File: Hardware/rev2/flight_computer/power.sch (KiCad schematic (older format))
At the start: 48 parts, among them U6 Buck_Converter_2, U7 LDO_600MA, U8 LP5907QMFX-3.3, U9 LP5907QMFX-3.3

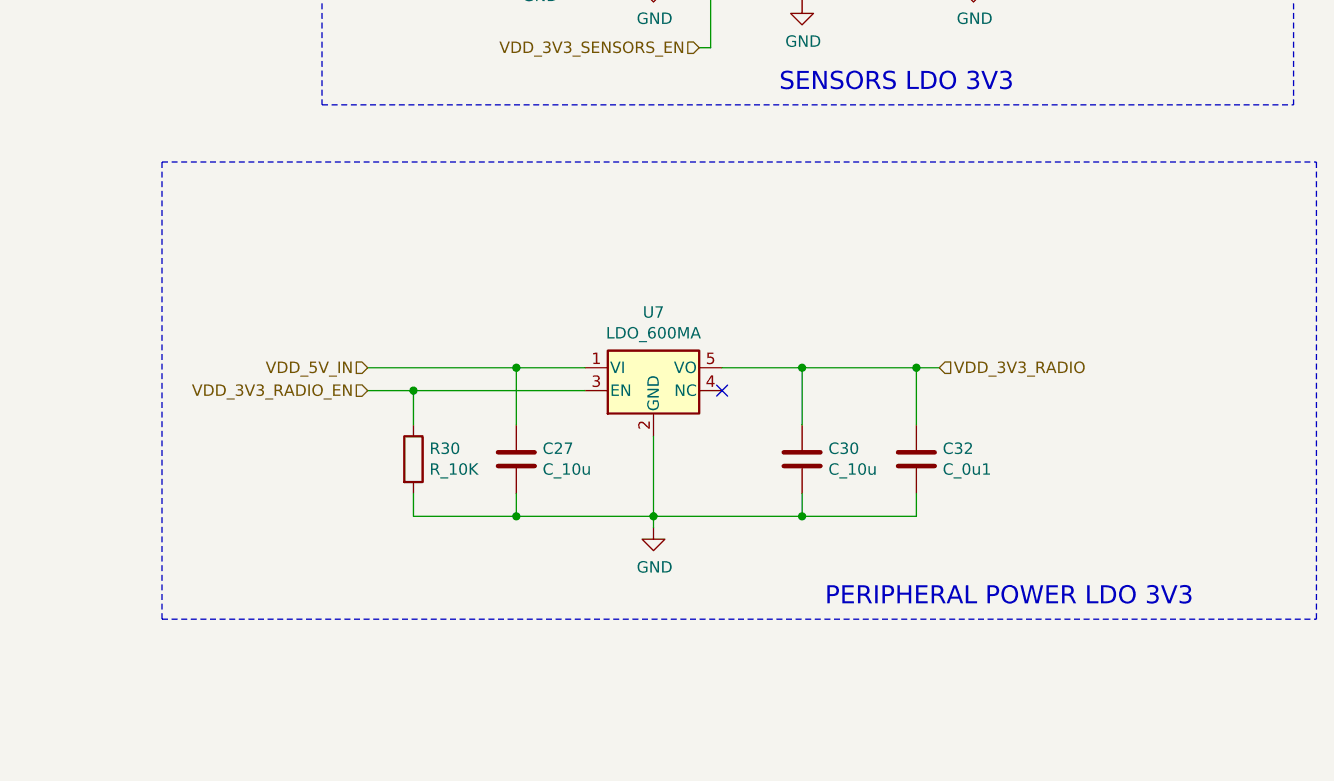
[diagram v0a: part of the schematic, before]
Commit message: Removes frysky + spektrum connectors
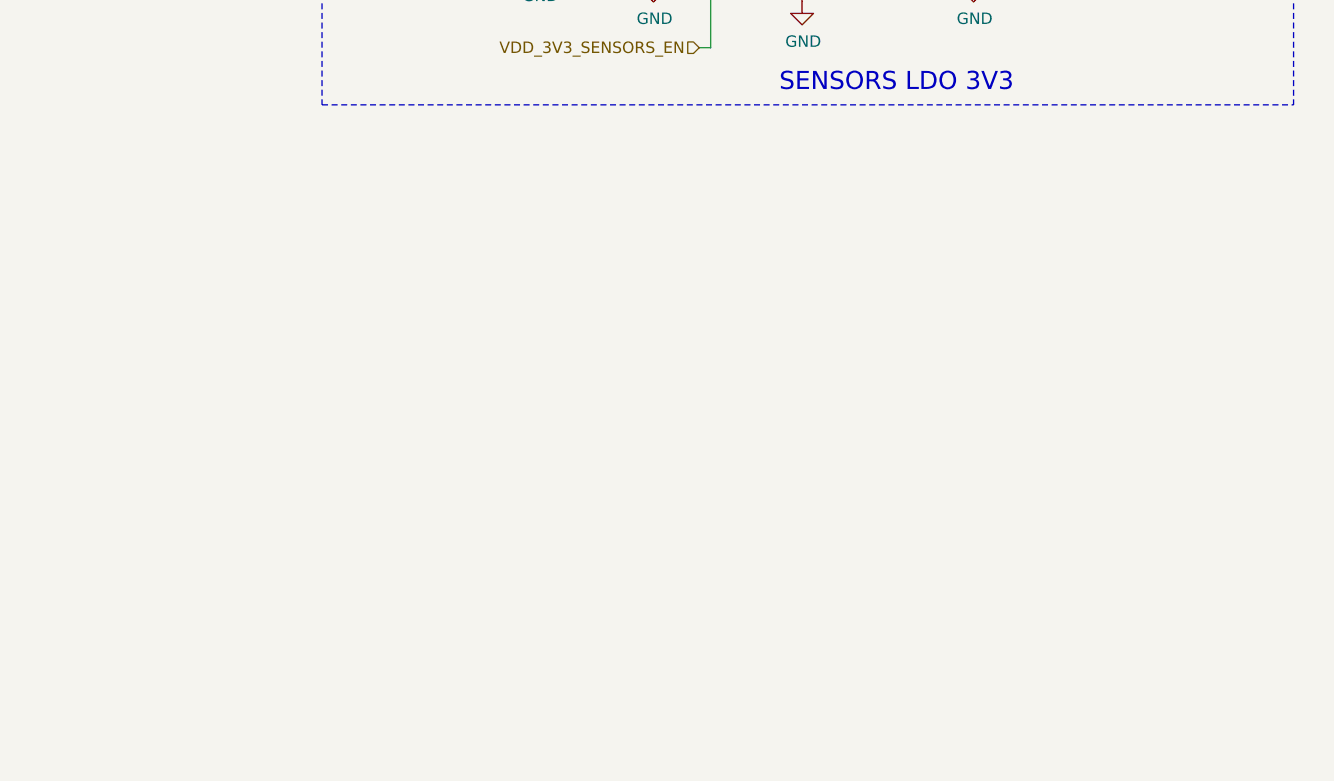
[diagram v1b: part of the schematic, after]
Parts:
- removed C27, C30: C_10u, Capacitors_SMD:C_0805, symbol openDrone_parts:C_10u
- removed C32: C_0u1, Capacitors_SMD:C_0805, symbol openDrone_parts:C_0u1
- removed R30: R_10K, Resistors_SMD:R_0805, symbol openDrone_parts:R_10K
- removed U7: LDO_600MA, drone_footprints:SOT-25_DIO, symbol openDrone_parts:LDO_600MA
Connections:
- no-connect marks 1 -> 0
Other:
- note removed: "PERIPHERAL POWER LDO 3V3"
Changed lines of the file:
@@
 	1    0    0    -1
 $EndComp
-$Comp
-L openDrone_parts:LDO_600MA U?
-U 1 1 5F8D4287
-P 12900 5300
-AR Path="/5F615F42/5F8D4287" Ref="U?"  Part="1"
-AR Path="/5F84A65B/5F8D4287" Ref="U7"  Part="1"
-F 0 "U7" H 12900 5542 50  0000 C CNN
-F 1 "LDO_600MA" H 12900 5451 50  0000 C CNN
-F 2 "drone_footprints:SOT-25_DIO" H 13400 5850 50  0001 C CIN
-F 3 "" H 12900 5250 50  0001 C CNN
-F 4 "AP7365-33WG-7DICT-ND" H 13300 5750 50  0001 C CNN "DPN"
-F 5 "AP7365-33WG-7" H 13300 5700 50  0001 C CNN "MPN"
-	1    12900 5300
-	1    0    0    -1
-$EndComp
-Text HLabel 11650 5300 0    50   Input ~ 0
-VDD_5V_IN
-$Comp
-L openDrone_parts:C_10u C?
-U 1 1 5F8D428F
-P 12300 5700
-AR Path="/5F615F42/5F8D428F" Ref="C?"  Part="1"
-AR Path="/5F84A65B/5F8D428F" Ref="C27"  Part="1"
-F 0 "C27" H 12415 5746 50  0000 L CNN
-F 1 "C_10u" H 12415 5655 50  0000 L CNN
-F 2 "Capacitors_SMD:C_0805" H 12338 5550 50  0001 C CNN
-F 3 "" H 12325 5800 50  0001 C CNN
-F 4 "490-16824-1-ND" H 12300 5700 60  0001 C CNN "DPN"
-	1    12300 5700
-	1    0    0    -1
-$EndComp
-$Comp
-L openDrone_parts:R_10K R?
-U 1 1 5F8D4296
-P 11850 5700
-AR Path="/5F615F42/5F8D4296" Ref="R?"  Part="1"
-AR Path="/5F84A65B/5F8D4296" Ref="R30"  Part="1"
-F 0 "R30" V 11804 5770 50  0000 L CNN
-F 1 "R_10K" V 11895 5770 50  0000 L CNN
-F 2 "Resistors_SMD:R_0805" H 11050 5850 50  0001 C CNN
-F 3 "" H 11550 6200 50  0001 C CNN
-F 4 "311-10.0KCRCT-ND" H 11200 5950 60  0001 C CNN "DPN"
-	1    11850 5700
-	0    1    1    0
-$EndComp
-$Comp
-L power:GND #PWR?
-U 1 1 5F8D429C
-P 12900 6000
-AR Path="/5F615F42/5F8D429C" Ref="#PWR?"  Part="1"
-AR Path="/5F84A65B/5F8D429C" Ref="#PWR043"  Part="1"
-F 0 "#PWR043" H 12900 5750 50  0001 C CNN
-F 1 "GND" H 12905 5827 50  0000 C CNN
-F 2 "" H 12900 6000 50  0001 C CNN
-F 3 "" H 12900 6000 50  0001 C CNN
-	1    12900 6000
-	1    0    0    -1
-$EndComp
-Wire Wire Line
-	12900 6000 12900 5950
-Wire Wire Line
-	12300 5850 12300 5950
-Wire Wire Line
-	12300 5950 12900 5950
-Connection ~ 12900 5950
-Wire Wire Line
-	12900 5950 12900 5600
-Wire Wire Line
-	11850 5850 11850 5950
-Wire Wire Line
-	11850 5950 12300 5950
-Connection ~ 12300 5950
-Wire Wire Line
-	11650 5300 12300 5300
-Wire Wire Line
-	12300 5550 12300 5300
-Connection ~ 12300 5300
-Wire Wire Line
-	12300 5300 12600 5300
-Wire Wire Line
-	11650 5400 11850 5400
-Wire Wire Line
-	11850 5550 11850 5400
-Connection ~ 11850 5400
-Wire Wire Line
-	11850 5400 12600 5400
-$Comp
-L openDrone_parts:C_10u C?
-U 1 1 5F8D42B4
-P 13550 5700
-AR Path="/5F615F42/5F8D42B4" Ref="C?"  Part="1"
-AR Path="/5F84A65B/5F8D42B4" Ref="C30"  Part="1"
-F 0 "C30" H 13665 5746 50  0000 L CNN
-F 1 "C_10u" H 13665 5655 50  0000 L CNN
-F 2 "Capacitors_SMD:C_0805" H 13588 5550 50  0001 C CNN
-F 3 "" H 13575 5800 50  0001 C CNN
-F 4 "490-16824-1-ND" H 13550 5700 60  0001 C CNN "DPN"
-	1    13550 5700
-	1    0    0    -1
-$EndComp
-$Comp
-L openDrone_parts:C_0u1 C?
-U 1 1 5F8D42BB
-P 14050 5700
-AR Path="/5F615F42/5F8D42BB" Ref="C?"  Part="1"
-AR Path="/5F84A65B/5F8D42BB" Ref="C32"  Part="1"
-F 0 "C32" H 14165 5746 50  0000 L CNN
-F 1 "C_0u1" H 14165 5655 50  0000 L CNN
-F 2 "Capacitors_SMD:C_0805" H 14088 5550 50  0001 C CNN
-F 3 "https://www.digikey.com/product-detail/en/kemet/C0805C104Z4VACTU/399-9159-1-ND/3522677" H 14075 5800 50  0001 C CNN
-F 4 "478-3352-1-ND" H 14050 5700 60  0001 C CNN "DPN"
-	1    14050 5700
-	1    0    0    -1
-$EndComp
-Wire Wire Line
-	13550 5850 13550 5950
-Wire Wire Line
-	13550 5950 12900 5950
-Wire Wire Line
-	14050 5850 14050 5950
-Wire Wire Line
-	14050 5950 13550 5950
-Connection ~ 13550 5950
-Wire Wire Line
-	13200 5300 13550 5300
-Wire Wire Line
-	14050 5300 14050 5550
-Wire Wire Line
-	13550 5550 13550 5300
-Connection ~ 13550 5300
-Wire Wire Line
-	13550 5300 14050 5300
-Text HLabel 14150 5300 2    50   Input ~ 0
-VDD_3V3_RADIO
 Text Notes 14850 2650 0    79   ~ 0
 STM LDO 3V3
@@
 Text HLabel 1350 3300 0    50   Input ~ 0
 VDD_5V_USB
-Text Notes 13650 6350 0    79   ~ 0
-PERIPHERAL POWER LDO 3V3
-Wire Notes Line
-	10750 4400 10750 6400
 Wire Notes Line
 	6350 750  6350 2550
@@
 Text Label 1350 4100 2    50   ~ 0
 VDD_5V_BUCK
-Wire Notes Line
-	10750 4400 15800 4400
-Wire Notes Line
-	10750 6400 15800 6400
-Wire Notes Line
-	15800 4400 15800 6400
-Text HLabel 11650 5400 0    50   Input ~ 0
-VDD_3V3_RADIO_EN
 Wire Wire Line
 	3850 1150 4000 1150
@@
 	4300 1250 4300 1150
 Connection ~ 4300 1150
-Connection ~ 14050 5300
-Wire Wire Line
-	14050 5300 14150 5300
 $Comp
 L openDrone_parts:LED_0805_Green D5
@@
 	0    1    1    0
 $EndComp
-NoConn ~ 13200 5400
 $EndSCHEMATC

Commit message: added new buck converter schematic
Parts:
- added C?: C_22u, drone_footprints:C_0805, symbol personal:C_22u
- added R?: R_2K18, personal:R_0805, symbol personal:R_2K18
- added U?: OKL-T_1-W12P-C, personal:OKL-T1-W12P-C, symbol personal:OKL-T_1-W12P-C
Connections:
- net GND: now also C?.2, R?.2, U?.11 (GND), U?.3 (GND), U?.7 (GND)
- net VBAT: now also C?.1, U?.2 (VIN)
- net VDD_5V_BUCK: now also U?.4 (VOUT)
- new net: R?.1, U?.6 (TRIM)
- no-connect marks 0 -> 1
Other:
- note added: "BUCK CONVERTER 5-14V, 2A"
- note added: "OLD BUCK CONVERTER 8-25V, 3A"
- note removed: "BUCK CONVERTER 8-25V, 3A"
- moved on the sheet: C18, C20, C21, C22, C23, C24, C25, L2, R15, R16, R23, R26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

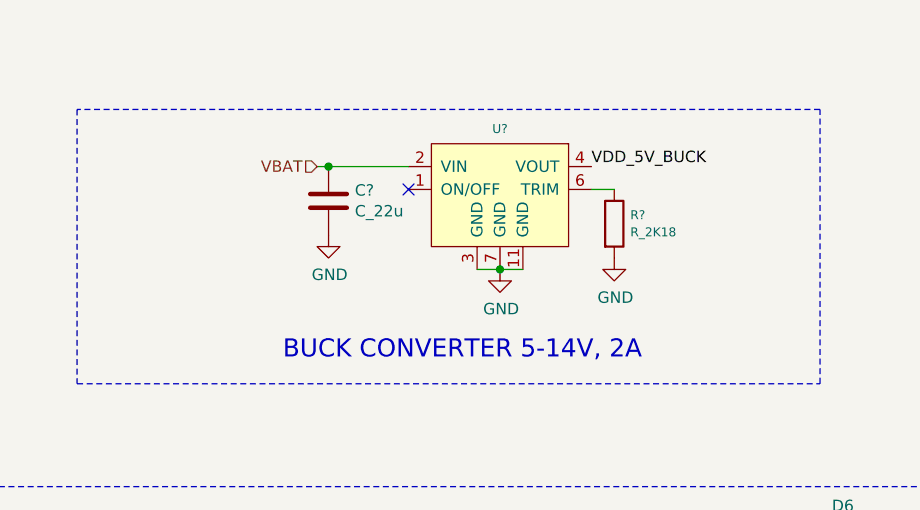
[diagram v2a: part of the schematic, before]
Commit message: added new buck converter
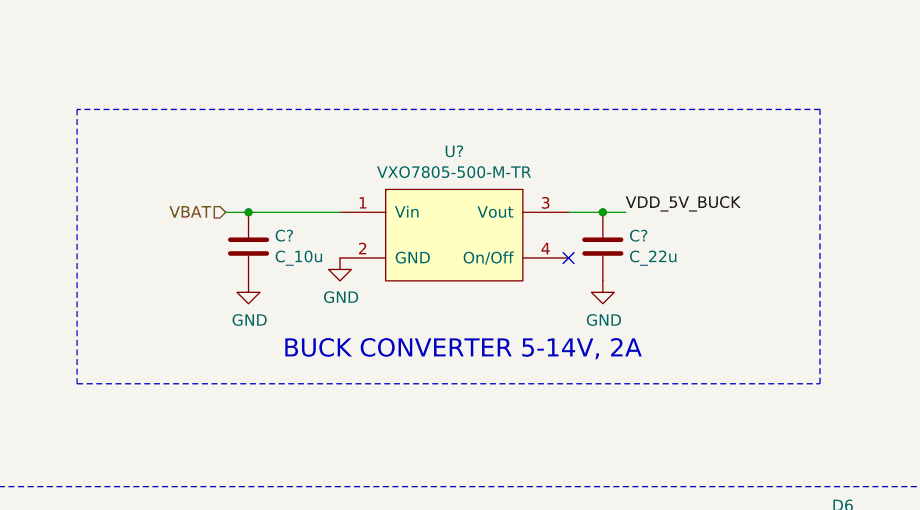
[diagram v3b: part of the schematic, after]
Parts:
- removed C?: C_22u, drone_footprints:C_0805, symbol personal:C_22u
- removed R?: R_2K18, personal:R_0805, symbol personal:R_2K18
- removed U?: OKL-T_1-W12P-C, personal:OKL-T1-W12P-C, symbol personal:OKL-T_1-W12P-C
- added C?: C_10u, drone_footprints:C_0805, symbol personal:C_10u
- added C?: C_22u, drone_footprints:C_0805, symbol personal:C_22u
- added U?: VXO7805-500-M-TR, personal:CONV_VXO7805-500-M, symbol personal:VXO7805-500-M-TR
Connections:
- net GND: now also C?.2, C?.2, U?.2 (GND)
- net VBAT: now also C?.1, U?.1 (Vin)
- net VDD_5V_BUCK: now also C?.1, U?.3 (Vout)
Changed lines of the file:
@@
 $EndComp
-$Comp
-L personal:C_22u C?
-U 1 1 600F4906
-P 3000 1600
-F 0 "C?" H 3115 1646 50  0000 L CNN
-F 1 "C_22u" H 3115 1555 50  0000 L CNN
-F 2 "drone_footprints:C_0805" H 3038 1450 50  0001 C CNN
-F 3 "" H 3025 1700 50  0001 C CNN
-F 4 "490-14661-1-ND" H 3000 1600 60  0001 C CNN "DPN"
-	1    3000 1600
-	1    0    0    -1
-$EndComp
-Wire Wire Line
-	3000 1450 3350 1450
-$Comp
-L personal:R_2K18 R?
-U 1 1 600F9361
-P 4250 1700
-F 0 "R?" V 4212 1770 39  0000 L CNN
-F 1 "R_2K18" V 4287 1770 39  0000 L CNN
-F 2 "personal:R_0805" H 4500 2150 39  0001 C CNN
-F 3 "" H 3950 2200 39  0001 C CNN
-F 4 "13-RT0805BRD072K18LCT-ND" H 4500 2050 39  0001 C CNN "DPN"
-F 5 "RT0805BRD072K18L" H 4550 1950 39  0001 C CNN "MPN"
-	1    4250 1700
-	0    1    1    0
-$EndComp
-Wire Wire Line
-	4150 1550 4250 1550
 $Comp
 L power:GND #PWR?
 U 1 1 600FE837
-P 4250 1850
-F 0 "#PWR?" H 4250 1600 50  0001 C CNN
-F 1 "GND" H 4255 1677 50  0000 C CNN
-F 2 "" H 4250 1850 50  0001 C CNN
-F 3 "" H 4250 1850 50  0001 C CNN
-	1    4250 1850
+P 3050 1850
+F 0 "#PWR?" H 3050 1600 50  0001 C CNN
+F 1 "GND" H 3055 1677 50  0000 C CNN
+F 2 "" H 3050 1850 50  0001 C CNN
+F 3 "" H 3050 1850 50  0001 C CNN
+	1    3050 1850
 	1    0    0    -1
 $EndComp
-$Comp
-L power:GND #PWR?
-U 1 1 600FE9E9
-P 3750 1900
-F 0 "#PWR?" H 3750 1650 50  0001 C CNN
-F 1 "GND" H 3755 1727 50  0000 C CNN
-F 2 "" H 3750 1900 50  0001 C CNN
-F 3 "" H 3750 1900 50  0001 C CNN
-	1    3750 1900
-	1    0    0    -1
-$EndComp
-Wire Wire Line
-	3650 1900 3750 1900
-Connection ~ 3750 1900
-Wire Wire Line
-	3750 1900 3850 1900
-NoConn ~ 3350 1550
-$Comp
-L power:GND #PWR?
-U 1 1 60107109
-P 3000 1750
-F 0 "#PWR?" H 3000 1500 50  0001 C CNN
-F 1 "GND" H 3005 1577 50  0000 C CNN
-F 2 "" H 3000 1750 50  0001 C CNN
-F 3 "" H 3000 1750 50  0001 C CNN
-	1    3000 1750
-	1    0    0    -1
-$EndComp
-Text Label 4150 1450 0    50   ~ 0
+Text Label 4300 1650 0    50   ~ 0
 VDD_5V_BUCK
-Text HLabel 2950 1450 0    50   Input ~ 0
+Text HLabel 2550 1650 0    50   Input ~ 0
 VBAT
-Wire Wire Line
-	2950 1450 3000 1450
-Connection ~ 3000 1450
-$Comp
-L personal:OKL-T_1-W12P-C U?
-U 1 1 6011A03E
-P 3750 1550
-F 0 "U?" H 3750 1815 39  0000 C CNN
-F 1 "OKL-T_1-W12P-C" H 3750 1800 39  0001 C CNN
-F 2 "personal:OKL-T1-W12P-C" H 4300 1900 39  0001 C CNN
-F 3 "https://www.murata.com/products/productdata/8807038124062/okl-t1-w12.pdf?1583754815000" H 3750 1550 39  0001 C CNN
-F 4 "811-3418-1-ND" H 4200 2000 39  0001 C CNN "DPN"
-F 5 "OKL-T/1-W12P-C" H 4200 1950 39  0001 C CNN "MPN"
-	1    3750 1550
-	1    0    0    -1
-$EndComp
 Text Notes 2800 2300 0    79   ~ 0
 BUCK CONVERTER 5-14V, 2A
@@
 Wire Notes Line
 	5150 1200 1900 1200
+$Comp
+L personal:VXO7805-500-M-TR U?
+U 1 1 600E9887
+P 3500 1650
+F 0 "U?" H 3550 1915 50  0000 C CNN
+F 1 "VXO7805-500-M-TR" H 3550 1824 50  0000 C CNN
+F 2 "personal:CONV_VXO7805-500-M" H 3600 2250 50  0001 C CNN
+F 3 "https://www.cui.com/product/resource/vxo78-500-m.pdf" H 3600 2250 50  0001 C CNN
+F 4 "102-VXO7805-500-M-CT-ND" H 3600 2150 50  0001 C CNN "DPN"
+F 5 "VXO7805-500-M-TR" H 3550 2050 50  0001 C CNN "MPN"
+	1    3500 1650
+	1    0    0    -1
+$EndComp
+NoConn ~ 4050 1850
+$Comp
+L power:GND #PWR?
+U 1 1 600F8543
+P 2650 1950
+F 0 "#PWR?" H 2650 1700 50  0001 C CNN
+F 1 "GND" H 2655 1777 50  0000 C CNN
+F 2 "" H 2650 1950 50  0001 C CNN
+F 3 "" H 2650 1950 50  0001 C CNN
+	1    2650 1950
+	1    0    0    -1
+$EndComp
+$Comp
+L power:GND #PWR?
+U 1 1 600FDDBC
+P 4200 1950
+F 0 "#PWR?" H 4200 1700 50  0001 C CNN
+F 1 "GND" H 4205 1777 50  0000 C CNN
+F 2 "" H 4200 1950 50  0001 C CNN
+F 3 "" H 4200 1950 50  0001 C CNN
+	1    4200 1950
+	1    0    0    -1
+$EndComp
+Wire Wire Line
+	2550 1650 2650 1650
+$Comp
+L personal:C_10u C?
+U 1 1 601035B1
+P 2650 1800
+F 0 "C?" H 2765 1846 50  0000 L CNN
+F 1 "C_10u" H 2765 1755 50  0000 L CNN
+F 2 "drone_footprints:C_0805" H 2688 1650 50  0001 C CNN
+F 3 "" H 2675 1900 50  0001 C CNN
+F 4 "490-16824-1-ND" H 2650 1800 60  0001 C CNN "DPN"
+	1    2650 1800
+	1    0    0    -1
+$EndComp
+Connection ~ 2650 1650
+Wire Wire Line
+	2650 1650 3050 1650
+Wire Wire Line
+	4050 1650 4200 1650
+$Comp
+L personal:C_22u C?
+U 1 1 60104712
+P 4200 1800
+F 0 "C?" H 4315 1846 50  0000 L CNN
+F 1 "C_22u" H 4315 1755 50  0000 L CNN
+F 2 "drone_footprints:C_0805" H 4238 1650 50  0001 C CNN
+F 3 "" H 4225 1900 50  0001 C CNN
+F 4 "490-14661-1-ND" H 4200 1800 60  0001 C CNN "DPN"
+	1    4200 1800
+	1    0    0    -1
+$EndComp
+Connection ~ 4200 1650
+Wire Wire Line
+	4200 1650 4300 1650
 $EndSCHEMATC
